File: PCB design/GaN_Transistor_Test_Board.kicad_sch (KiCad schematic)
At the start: 4 parts, among them Q1 IGD70R500D2S

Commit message: Layout redesign
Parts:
- added J1, J2, J3, J4: Conn_01x01, symbol Connector_Generic:Conn_01x01
- added R1: R, Resistor_SMD:R_0805_2012Metric_Pad1.20x1.40mm_HandSolder, symbol Device:R
- added R2: 100, Resistor_SMD:R_0805_2012Metric_Pad1.20x1.40mm_HandSolder, symbol Device:R
- added TVS1: D_Zener, Footprints:SMFSeries_LTF, symbol Device:D_Zener
- Q1: footprint Footprints:TO-252-3_TabPin4 -> Footprints:IFX-PG-TO252-3N-37-V1
- renumbered E3 to D1, E1 to G1, E2 to S1
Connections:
- net GND: now also Q1.2 (S), S1.1 (SIG), J3.1 (Pin_1), J4.1 (Pin_1), TVS1.1 (K)
- net at Q1.1 (G): now also R2.1, TVS1.2 (A); no longer G1.1 (SIG)
- net at D1.1 (SIG): now also J1.1 (Pin_1), R1.1; no longer Q1.3 (D)
- new net: G1.1 (SIG), J2.1 (Pin_1), R2.2
- new net: Q1.3 (D), R1.2
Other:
- company: (none) -> eng. Mateusz Witczak
- title: (none) -> GaN Transistor Test Board
- moved on the sheet: D1, G1, S1

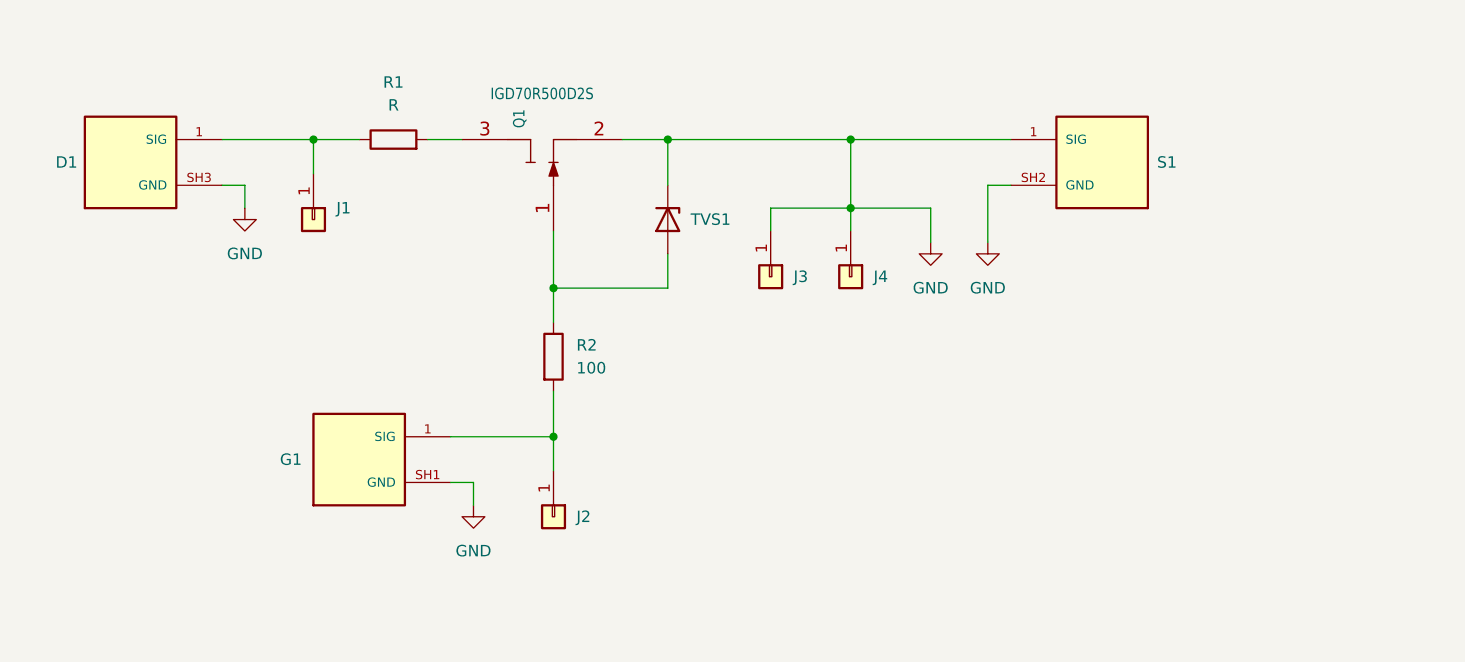
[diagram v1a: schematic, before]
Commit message: Add test points
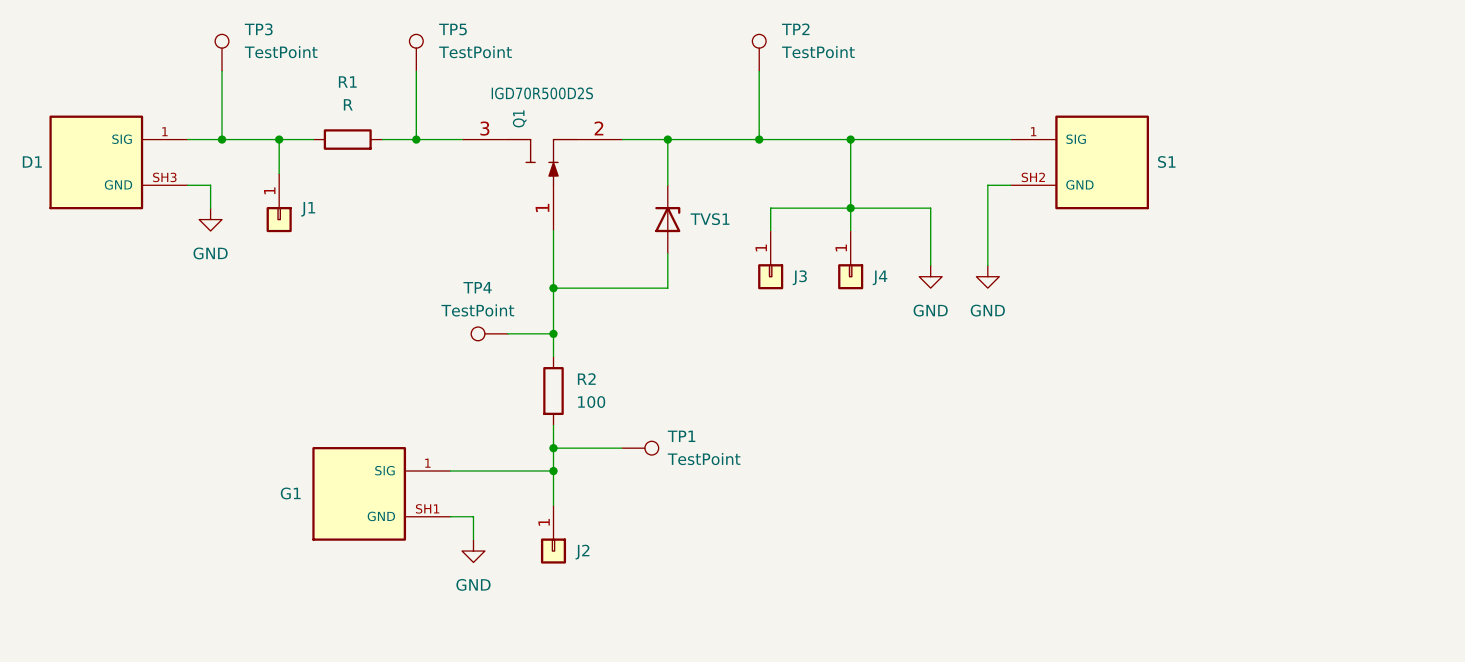
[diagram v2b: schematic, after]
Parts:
- added TP1, TP2, TP3, TP4, TP5: TestPoint, symbol Connector:TestPoint
- J1, J2, J3, J4: footprint (none) -> Footprints:CONN1_FCR7350R_CLF
- R1: footprint Resistor_SMD:R_0805_2012Metric_Pad1.20x1.40mm_HandSolder -> (none)
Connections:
- net GND: now also TP2.1
- net at Q1.1 (G), R2.1, TVS1.2 (A): now also TP4.1
- net at G1.1 (SIG), J2.1 (Pin_1), R2.2: now also TP1.1
- net at D1.1 (SIG), J1.1 (Pin_1), R1.1: now also TP3.1
- net at Q1.3 (D), R1.2: now also TP5.1
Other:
- moved on the sheet: D1, G1, J1, J2, R1, R2

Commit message: Simulation PCB update v1
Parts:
- added TP6: TestPoint, symbol Connector:TestPoint
- R1: value R -> 680
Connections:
- net GND: now also TP6.1
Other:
- moved on the sheet: D1, G1, J1, J2, J3, J4, Q1, R1, R2, S1, TP1, TP2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
